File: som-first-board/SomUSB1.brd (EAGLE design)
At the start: 30.5 x 72.5 mm, 22 parts, among them U1 MP2122

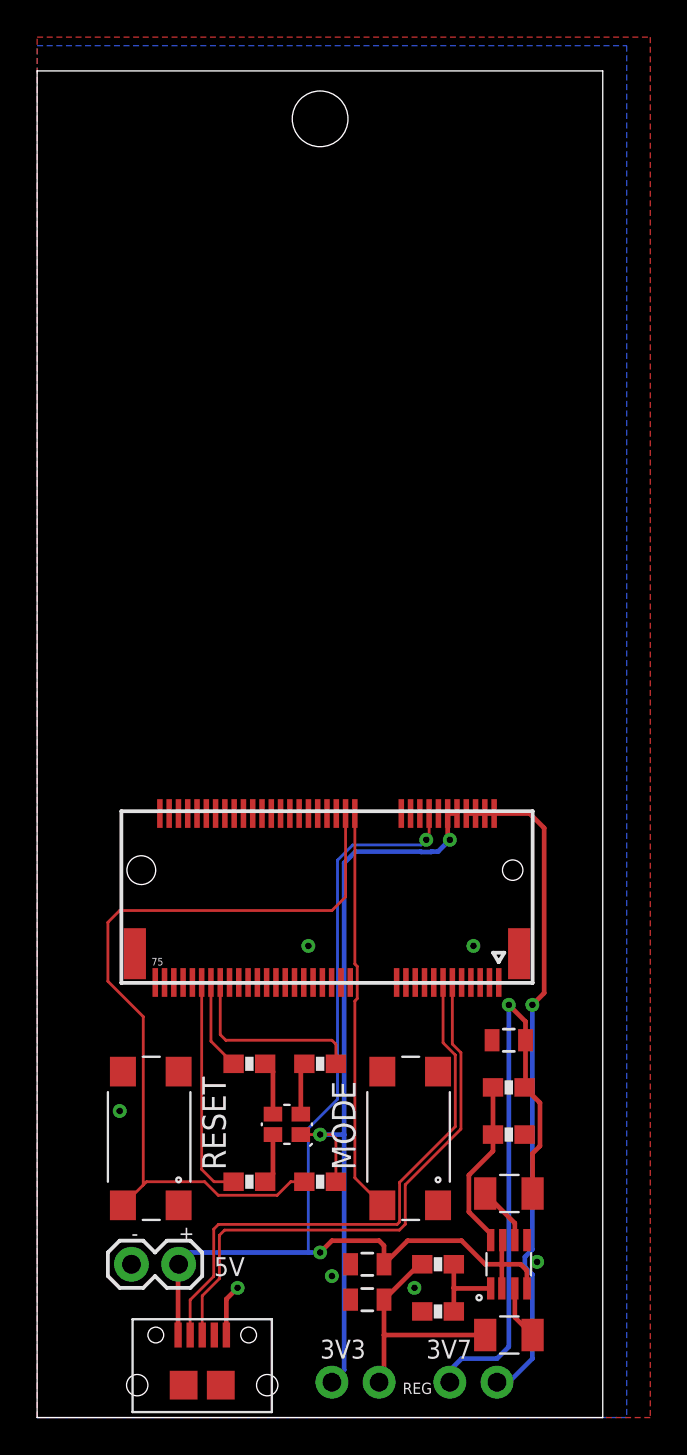
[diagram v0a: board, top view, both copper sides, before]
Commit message: Update M.2 standoff
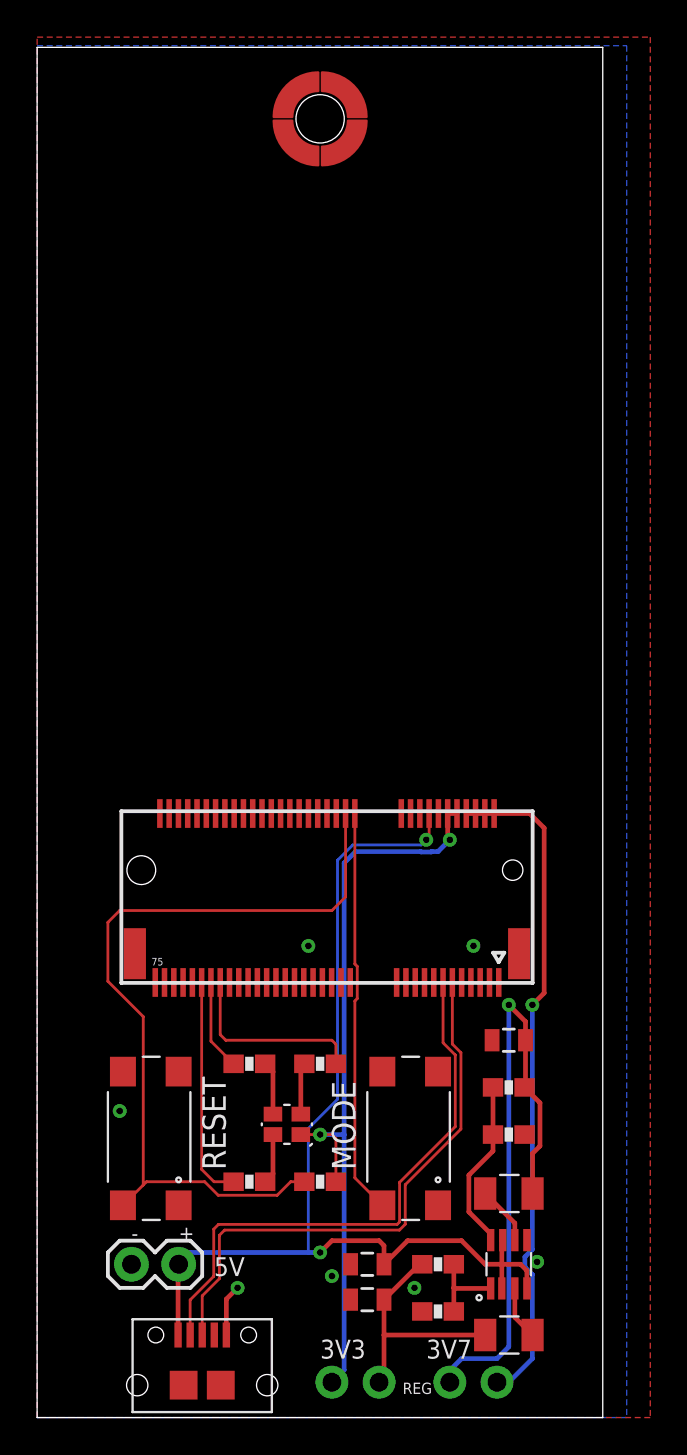
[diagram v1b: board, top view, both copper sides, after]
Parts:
- added U$1: M2-STANDOFF, rickk2:M2-STANDOFF
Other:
- board size 30.5 x 72.5 mm -> 30.5 x 73.8 mm
- board text added: "SomUSB1 v4"
- board text removed: "SomUSB1 v3"
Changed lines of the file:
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@@
 <plain>
 <wire x1="0" y1="0" x2="30.46" y2="0" width="0" layer="20"/>
-<wire x1="30.46" y1="0" x2="30.46" y2="72.52" width="0" layer="20"/>
-<wire x1="30.46" y1="72.52" x2="0" y2="72.52" width="0" layer="20"/>
-<wire x1="0" y1="72.52" x2="0" y2="0" width="0" layer="20"/>
+<wire x1="30.46" y1="0" x2="30.46" y2="73.79" width="0" layer="20"/>
+<wire x1="30.46" y1="73.79" x2="0" y2="73.79" width="0" layer="20"/>
+<wire x1="0" y1="73.79" x2="0" y2="0" width="0" layer="20"/>
 <text x="10.16" y="13.335" size="1.27" layer="21" rot="R90">RESET</text>
 <text x="17.145" y="13.335" size="1.27" layer="21" rot="R90">MODE</text>
 <text x="19.05" y="34.29" size="1.27" layer="22" rot="MR0">SomUSB1
-v3</text>
+v4</text>
 <text x="15.24" y="3.175" size="1.016" layer="21">3V3</text>
 <text x="20.955" y="3.175" size="1.016" layer="21">3V7</text>
@@
 <text x="7.62" y="9.525" size="0.8128" layer="21">+</text>
 <text x="5.08" y="9.525" size="0.8128" layer="21">-</text>
-<hole x="15.24" y="69.94" drill="3"/>
 <dimension x1="15.24" y1="27.94" x2="15.24" y2="69.94" x3="0.54" y3="48.94" textsize="1.778" layer="48"/>
 </plain>
@@
 <element name="SJ2" library="rickk2" package="PTH-JUMPER-2-NO_NO_SILK" value="JUMPER-PTH-2-NO" x="23.495" y="1.905" smashed="yes"/>
 <element name="JP1" library="rickk2" package="1X02" value="M02PTH" x="5.08" y="8.255" smashed="yes"/>
+<element name="U$1" library="rickk2" package="M2-STANDOFF" value="M2-STANDOFF" x="15.24" y="69.94" smashed="yes"/>
 </elements>
 <signals>
